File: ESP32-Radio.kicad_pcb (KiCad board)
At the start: 2 copper layers, 119.8 x 71.5 mm, 67 parts, among them J1 Jack-DC, J11 Conn_01x04_Female, J2 BNC, J6 Audio_Jack, Q1 2N3904-SMD, Q2 2SC5706, Q3 2SC5706, T1 T37_XFRM, U1 LM358, U10 si5351, U11 LD33V, U2 LM358, U6 MCP1703A-2502_SOT223, U8 FST3253

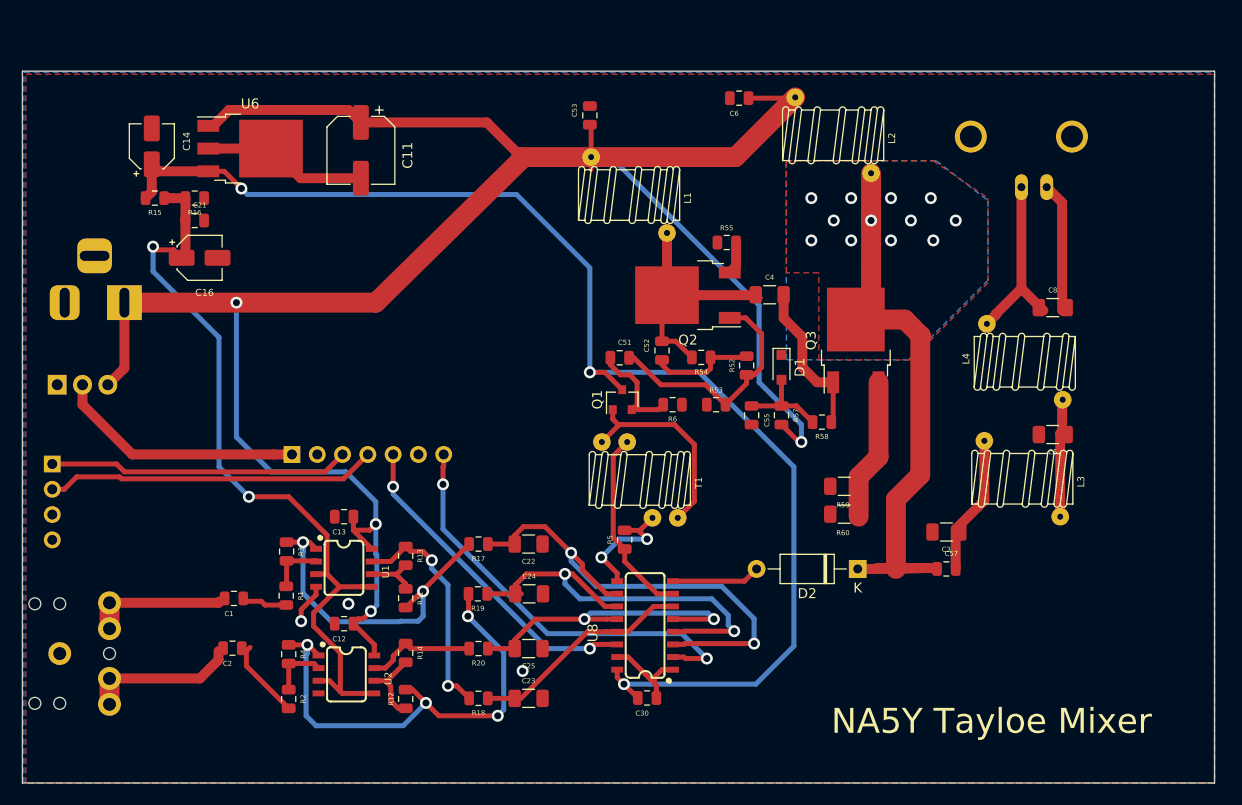
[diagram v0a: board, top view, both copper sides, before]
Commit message: added trap to lowpass
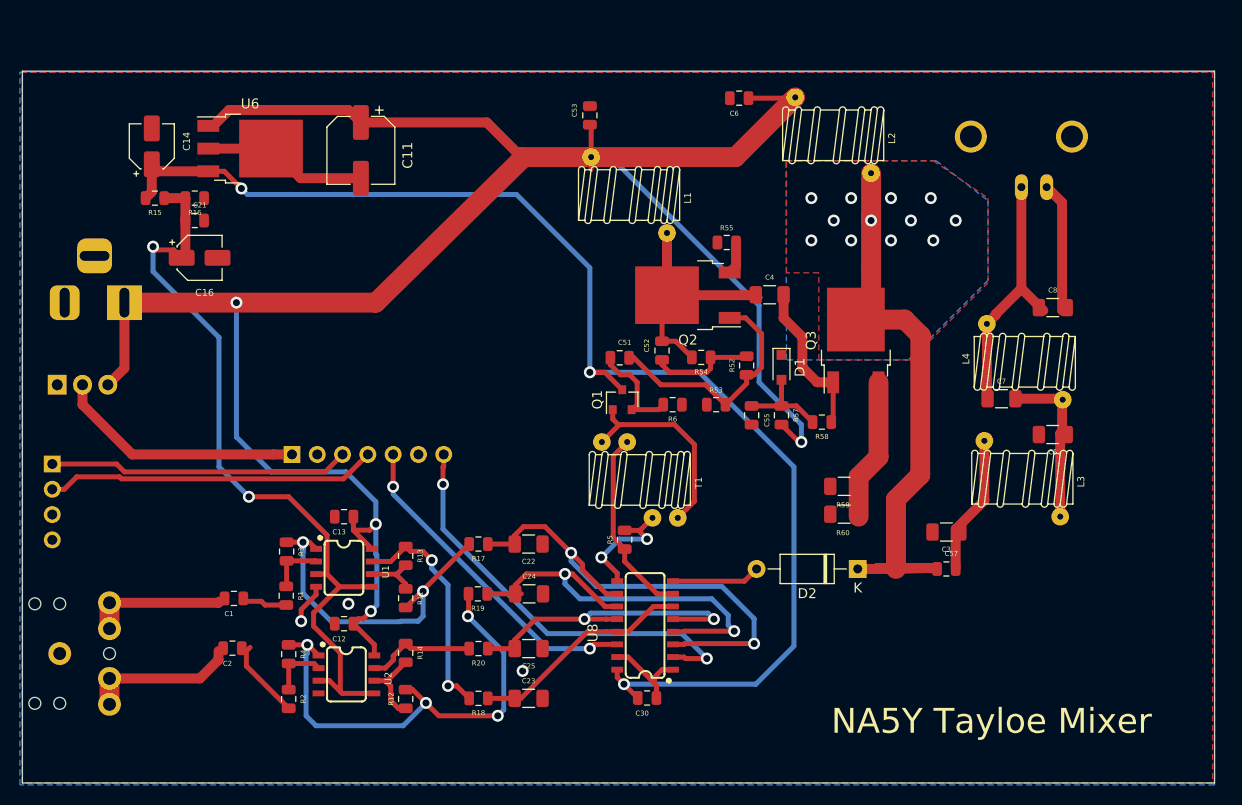
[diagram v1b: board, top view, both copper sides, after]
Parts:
- added C7: 33p, Xenir:Capacitor 1206, F.Cu at (244.6, 123.2)
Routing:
- net Net-(C7-Pad1): track 18.3 -> 25.8 mm
- net Net-(C5-Pad1): track 11.9 -> 16.6 mm

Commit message: fixed rescue reference
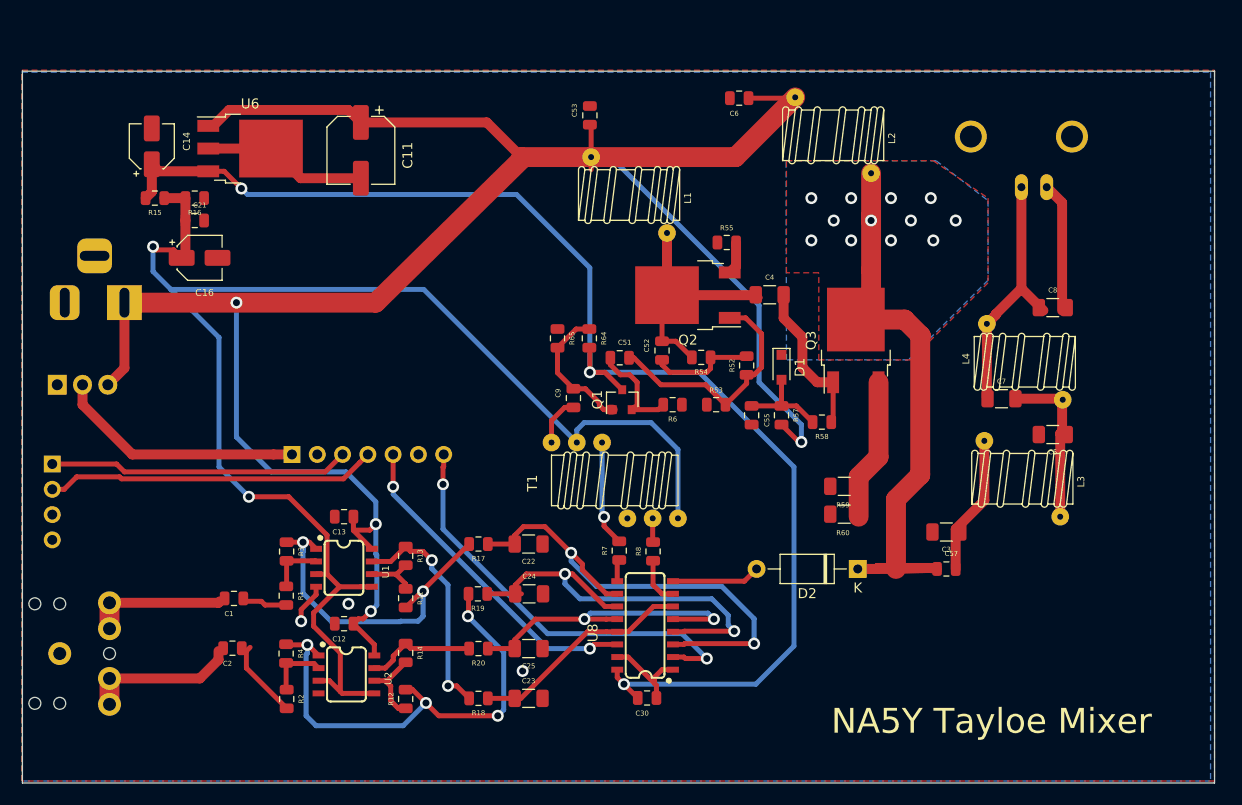
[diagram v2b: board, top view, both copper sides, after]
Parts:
- removed R5: 1k, Xenir:Resistor 0805
- added C9: .1uF, Xenir:Capacitor 0805, F.Cu at (199.1, 125.3)
- added R64: 4.7k, Xenir:Resistor 0805, F.Cu at (200.7, 119.3)
- added R65: 4.7k, Xenir:Resistor 0805, F.Cu at (197.5, 119.3)
- added R7: 49.9, Xenir:Resistor 0805, F.Cu at (208.7, 140.7)
- added R8: 49.9, Xenir:Resistor 0805, F.Cu at (212.1, 140.7)
- T1: value T37_XFRM -> T50_SPLITTER; footprint Xenir:T37 Transformer -> Xenir:T50 Trifilar
- moved T1 18.3 mm to (197.0, 133.9), turned to 90 degrees
- moved R4 0.27 mm to (170.2, 151.0)
- moved R2 0.20 mm to (170.3, 155.6)
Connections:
- Q1 pad 1: Net-(Q1-Pad1) -> Net-(C9-Pad2)
- T1 pad C1A: Net-(Q1-Pad1) -> Net-(C9-Pad1)
- T1 pad C1B: Net-(R5-Pad1) -> GND
- T1 pad C2A: Net-(R5-Pad2) -> +2V5
- T1 pad C2B: Net-(Q1-Pad1) -> Net-(R8-Pad1)
- U8 pad 7: Net-(R5-Pad2) -> Net-(R8-Pad2)
- U8 pad 9: Net-(R5-Pad1) -> Net-(R7-Pad2)
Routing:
- net +2V5: track 79.2 -> 146.2 mm
- net Net-(Q1-Pad1): track 21.0 -> 0.00 mm
- net Net-(R5-Pad2): track 19.3 -> 0.00 mm
- net Net-(C9-Pad2): track 0.00 -> 14.0 mm
- net Net-(R5-Pad1): track 13.0 -> 0.00 mm, vias 2 -> 0
- net Net-(R7-Pad1): track 0.00 -> 10.6 mm, vias 0 -> 1
- net Net-(C9-Pad1): track 0.00 -> 4.95 mm
- net Net-(R8-Pad2): track 0.00 -> 4.80 mm
- net +5V: track 131.2 -> 133.7 mm
- net Net-(R8-Pad1): track 0.00 -> 2.40 mm
- net Net-(R7-Pad2): track 0.00 -> 2.21 mm

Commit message: created
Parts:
- removed C21, C51, C52, C55: .1uF, Xenir:Capacitor 0805
- removed C4: 150pF, Xenir:Capacitor 1206
- removed C7: 33p, Xenir:Capacitor 1206
- removed D2: D_Zener, Diode_THT:D_A-405_P10.16mm_Horizontal
- removed L2: Inductor, Xenir:T37_Inductor
- removed R54: 10k, Xenir:Resistor 0805
- removed R55: 10, Xenir:Resistor 0805
- removed R57: 1k, Xenir:Resistor 0805
- removed R58: 100, Xenir:Resistor 0805
- removed R59, R60: 1, Xenir:Resistor 1206
- removed U11: LD33V, Package_TO_SOT_THT:TO-220-3_Vertical
- added C103: .1uF, Xenir:Capacitor 0805, F.Cu at (184.5, 107.9)
- added C104: .1uF, Xenir:Capacitor 0805, F.Cu at (230.9, 104.8)
- added C110: .1uF, Xenir:Capacitor 0805, F.Cu at (219.9, 109.2)
- added C112: .1uF, Xenir:Capacitor 0805, F.Cu at (201.8, 116.4)
- added C15: .1uF, Xenir:Capacitor 0805, F.Cu at (193.0, 113.9)
- added C17: .1uF, Xenir:Capacitor 0805, F.Cu at (177.7, 110.0)
- added C18: 22uF, Xenir:Cap_4x5.4, F.Cu at (175.3, 112.9)
- added C19: .1uF, Xenir:Capacitor 0805, F.Cu at (173.4, 113.5)
- added C201: .1uF, Xenir:Capacitor 0805, F.Cu at (204.7, 113.1)
- added C202: .1uF, Xenir:Capacitor 0805, F.Cu at (206.2, 112.5)
- added C207: 33p, Xenir:Capacitor 1206, F.Cu at (249.8, 114.3)
- added J4: Audio_Jack, Xenir:Audio_Jack, B.Cu at (151.9, 121.9)
- added Q4: IRF510, Package_TO_SOT_THT:TO-220-3_Vertical, F.Cu at (229.9, 128.1)
- added Q5: IRFU9024, Package_TO_SOT_THT:TO-251-3_Vertical, F.Cu at (159.3, 114.8)
- added R101: 18, Xenir:Resistor 0805, F.Cu at (197.7, 108.9)
- added R102: 18, Xenir:Resistor 0805, F.Cu at (193.1, 111.4)
- added R108: 100, Xenir:Resistor 0805, F.Cu at (204.7, 110.4)
- added R110: 62, Xenir:Resistor 0805, F.Cu at (205.6, 122.8)
- added R201: 33, Xenir:Resistor 0805, F.Cu at (204.8, 115.9)
- added R202: 10, Xenir:Resistor 0805, F.Cu at (214.7, 112.6)
- added R209: 2.7k, Xenir:Resistor 0805, F.Cu at (211.2, 107.0)
- added R93: 10k, Xenir:Resistor 0805, F.Cu at (154.3, 119.5)
- added R94: 10k, Xenir:Resistor 0805, F.Cu at (161.5, 120.4)
- added R95: 1.5k, Xenir:Resistor 0805, F.Cu at (154.3, 127.5)
- added R97: 10k, Xenir:Resistor 0805, F.Cu at (160.5, 118.5)
- added RV1: R_POT, Xenir:Trimpot Vertical, F.Cu at (210.3, 126.0)
- added RV2: R_POT, Xenir:Trimpot Vertical, F.Cu at (214.8, 101.7)
- added T12: T37-43 25T:8T, Xenir:T37 Transformer, F.Cu at (173.5, 121.5)
- added T13: T37-43 8T:4T, Xenir:T37 Transformer, F.Cu at (196.3, 100.3)
- added U3: AMS1117, Package_TO_SOT_SMD:SOT-223-3_TabPin2, F.Cu at (169.6, 124.3)
- C203: renamed from C3; value 220pF -> 150p
- C205: renamed from C5; value 470pF -> 330p
- C208: renamed from C8; value 330pF -> 150p
- D1: value 1N914 -> D_Zener; footprint Diode_SMD:D_SOD-323_HandSoldering -> Diode_SMD:D_MiniMELF
- L1: value Inductor -> T50-43 10T; footprint Xenir:T37_Inductor -> Xenir:T50_Inductor
- L3: value 10T T37-6 -> 14T T37-6
- L4: value 11T T37-6 -> 18T T37-6
- Q3: value 2SC5706 -> BS170F; footprint Package_TO_SOT_SMD:TO-252-2 -> Package_TO_SOT_SMD:SOT-23
- R106: renamed from R6; value 100 -> 62
- R52: value 1k -> 24k
- R53: value 1k -> 6.8k
- R64: value 4.7k -> 24k
- R65: value 4.7k -> 6.8k
- moved Q3 69.8 mm to (160.3, 124.4)
- moved C6 64.2 mm to (160.3, 125.3), turned to 0 degrees
- moved R52 40.5 mm to (182.4, 111.5), turned to 0 degrees
- moved R53 34.0 mm to (186.5, 111.5), turned to 0 degrees
- moved L1 27.5 mm to (241.0, 111.1)
- moved Q2 23.9 mm to (191.8, 104.2), turned to 90 degrees
- moved J1 22.0 mm to (156.4, 93.8)
- moved C11 21.5 mm to (168.7, 88.0), turned to 0 degrees
- moved C203 19.7 mm to (253.0, 127.0), turned to 0 degrees
- moved D1 18.8 mm to (210.3, 107.9), turned to 0 degrees
- moved C14 18.3 mm to (177.0, 101.7)
- moved R16 15.4 mm to (167.7, 117.5), turned to 180 degrees
- moved C57 14.9 mm to (246.1, 126.8)
- moved Q1 13.2 mm to (194.2, 120.6)
- moved L3 12.2 mm to (262.6, 125.1)
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- renumbered R7 to R147, R8 to R148
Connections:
- C16 pad 1: +2V5 -> 12V-On
- C53 pad 1: +12V -> 12V-On
- C6 pad 1: +12V -> Net-(C6-Pad1)
- D1 pad 1: GND -> Net-(C202-Pad2)
- L1 pad 2: Net-(C4-Pad1) -> Net-(C57-Pad1)
- Q1 pad 3: +5V -> Net-(Q1-Pad3)
- Q2 pad 2: Net-(C4-Pad1) -> Net-(Q2-Pad2)
- Q3 pad 1: Net-(C4-Pad2) -> Net-(C6-Pad1)
- Q3 pad 2: Net-(C57-Pad1) -> GND
- R52 pad 1: Net-(C52-Pad1) -> 12V-On
- R64 pad 1: +5V -> 12V-On
- T1 pad C1A: Net-(C9-Pad1) -> Net-(RV1-Pad1)
- U6 pad 1: +12V -> 12V-On
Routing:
- net +5V: track 133.7 -> 3.69 mm, vias 3 -> 1
- net +12V: track 224.2 -> 113.6 mm, vias 4 -> 2
- net +2V5: track 146.2 -> 54.2 mm, vias 2 -> 0
- net Net-(C57-Pad1): track 62.2 -> 14.6 mm, vias 12 -> 0
- net GND: track 51.8 -> 13.3 mm
- net Net-(C4-Pad1): track 33.2 -> 0.00 mm
- net Net-(C207-Pad1): track 25.8 -> 0.00 mm
- net +3V3: track 25.1 -> 0.00 mm
- net Net-(C103-Pad2): track 24.6 -> 0.00 mm
- net Net-(C205-Pad1): track 16.6 -> 0.00 mm
- net Net-(C4-Pad2): track 15.9 -> 0.00 mm
- net Net-(Q3-Pad3): track 14.3 -> 0.00 mm
- net Net-(C203-Pad1): track 14.1 -> 0.00 mm
- net Net-(C9-Pad2): track 14.0 -> 0.00 mm
- net Net-(C112-Pad1): track 10.7 -> 0.00 mm
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- removed copper zone on B.Cu, net GND
- removed copper zone on F.Cu, net GND
- removed copper zone on B.Cu, net Net-(C57-Pad1)
- removed copper zone on F.Cu, net Net-(C57-Pad1)
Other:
- board outline removed
